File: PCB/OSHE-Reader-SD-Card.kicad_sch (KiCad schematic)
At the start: 3 parts, among them J2 112L-TDA0

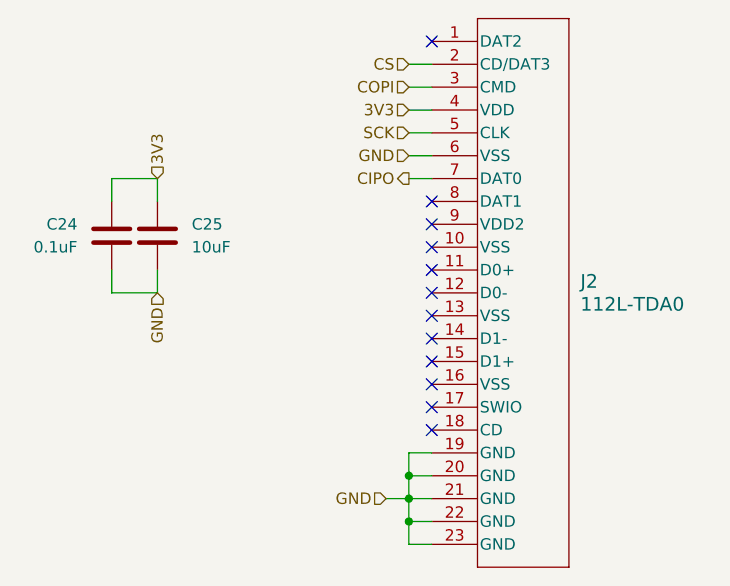
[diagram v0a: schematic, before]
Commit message: fixed battery voltage input to mcu being over 3.3V, minor changes to layout of sd card schematic
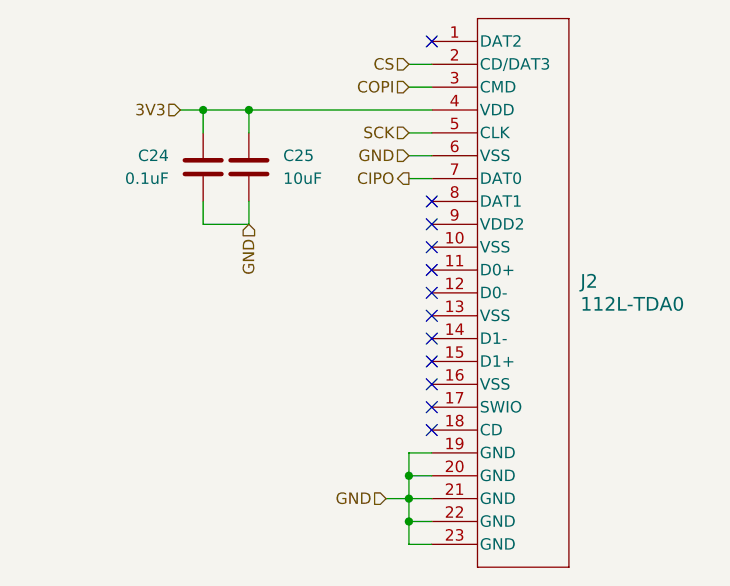
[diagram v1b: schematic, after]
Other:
- moved on the sheet: C24, C25
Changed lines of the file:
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@@
 	(paper "A4")
+	(junction
+		(at 49.53 57.15)
+		(diameter 0)
+		(color 0 0 0 0)
+	)
 	(junction
 		(at 72.39 97.79)
@@
 	)
 	(junction
+		(at 54.61 57.15)
+		(diameter 0)
+		(color 0 0 0 0)
+	)
+	(junction
 		(at 72.39 100.33)
 		(diameter 0)
@@
 	(wire
 		(pts
-			(xy 44.45 74.93) (xy 44.45 77.47)
+			(xy 49.53 67.31) (xy 49.53 69.85)
+		)
+		(stroke
+			(width 0)
+			(type default)
+		)
+	)
+	(wire
+		(pts
+			(xy 49.53 57.15) (xy 54.61 57.15)
 		)
 		(stroke
@@
 	(wire
 		(pts
-			(xy 39.37 67.31) (xy 39.37 64.77)
+			(xy 54.61 57.15) (xy 74.93 57.15)
 		)
 		(stroke
@@
 	(wire
 		(pts
-			(xy 39.37 77.47) (xy 44.45 77.47)
-		)
-		(stroke
-			(width 0)
-			(type default)
-		)
-	)
-	(wire
-		(pts
 			(xy 69.85 100.33) (xy 72.39 100.33)
 		)
@@
 	(wire
 		(pts
-			(xy 39.37 64.77) (xy 44.45 64.77)
+			(xy 54.61 67.31) (xy 54.61 69.85)
 		)
 		(stroke
@@
 	(wire
 		(pts
-			(xy 72.39 57.15) (xy 74.93 57.15)
-		)
-		(stroke
-			(width 0)
-			(type default)
-		)
-	)
-	(wire
-		(pts
-			(xy 44.45 64.77) (xy 44.45 67.31)
+			(xy 49.53 69.85) (xy 54.61 69.85)
+		)
+		(stroke
+			(width 0)
+			(type default)
+		)
+	)
+	(wire
+		(pts
+			(xy 54.61 57.15) (xy 54.61 59.69)
+		)
+		(stroke
+			(width 0)
+			(type default)
+		)
+	)
+	(wire
+		(pts
+			(xy 49.53 59.69) (xy 49.53 57.15)
+		)
+		(stroke
+			(width 0)
+			(type default)
+		)
+	)
+	(wire
+		(pts
+			(xy 46.99 57.15) (xy 49.53 57.15)
 		)
 		(stroke
@@
 	(wire
 		(pts
-			(xy 39.37 74.93) (xy 39.37 77.47)
-		)
-		(stroke
-			(width 0)
-			(type default)
-		)
-	)
-	(wire
-		(pts
 			(xy 72.39 59.69) (xy 74.93 59.69)
 		)
@@
 		)
 	)
+	(hierarchical_label "GND"
+		(shape input)
+		(at 54.61 69.85 270)
+		(effects
+			(font
+				(size 1.27 1.27)
+			)
+			(justify right)
+		)
+	)
 	(hierarchical_label "CS"
 		(shape input)
@@
 		)
 	)
-	(hierarchical_label "3V3"
-		(shape input)
-		(at 44.45 64.77 90)
-		(effects
-			(font
-				(size 1.27 1.27)
-			)
-			(justify left)
-		)
-	)
 	(hierarchical_label "GND"
 		(shape input)
@@
 		(shape input)
 		(at 69.85 100.33 180)
-		(effects
-			(font
-				(size 1.27 1.27)
-			)
-			(justify right)
-		)
-	)
-	(hierarchical_label "GND"
-		(shape input)
-		(at 44.45 77.47 270)
 		(effects
 			(font
@@
 	(hierarchical_label "3V3"
 		(shape input)
-		(at 72.39 57.15 180)
+		(at 46.99 57.15 180)
 		(effects
 			(font
@@
 	(symbol
 		(lib_id "Device:C")
-		(at 39.37 71.12 0)
+		(at 49.53 63.5 0)
 		(mirror y)
 		(unit 1)
@@
 		(dnp no)
 		(property "Reference" "C24"
-			(at 35.56 69.8499 0)
+			(at 45.72 62.2299 0)
 			(effects
 				(font
@@
 		)
 		(property "Value" "0.1uF"
-			(at 35.56 72.3899 0)
+			(at 45.72 64.7699 0)
 			(effects
 				(font
@@
 		)
 		(property "Footprint" ""
-			(at 38.4048 74.93 0)
+			(at 48.5648 67.31 0)
 			(effects
 				(font
@@
 		)
 		(property "Datasheet" "~"
-			(at 39.37 71.12 0)
+			(at 49.53 63.5 0)
 			(effects
 				(font
@@
 		)
 		(property "Description" "Unpolarized capacitor"
-			(at 39.37 71.12 0)
+			(at 49.53 63.5 0)
 			(effects
 				(font
@@
 	(symbol
 		(lib_id "Device:C")
-		(at 44.45 71.12 0)
+		(at 54.61 63.5 0)
 		(unit 1)
 		(exclude_from_sim no)
@@
 		(fields_autoplaced yes)
 		(property "Reference" "C25"
-			(at 48.26 69.8499 0)
+			(at 58.42 62.2299 0)
 			(effects
 				(font
@@
 		)
 		(property "Value" "10uF"
-			(at 48.26 72.3899 0)
+			(at 58.42 64.7699 0)
 			(effects
 				(font
@@
 		)
 		(property "Footprint" ""
-			(at 45.4152 74.93 0)
+			(at 55.5752 67.31 0)
 			(effects
 				(font
@@
 		)
 		(property "Datasheet" "~"
-			(at 44.45 71.12 0)
+			(at 54.61 63.5 0)
 			(effects
 				(font
@@
 		)
 		(property "Description" "Unpolarized capacitor"
-			(at 44.45 71.12 0)
+			(at 54.61 63.5 0)
 			(effects
 				(font
@@
 		)
 		(instances
-			(project ""
+			(project "OSHE-Reader-PCB"
 				(path "/3f072c92-e35a-4654-839b-728bd3dc3a46/f673c940-d558-4160-83eb-d33ca6356616"
 					(reference "C25")

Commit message: Footprints added
All footprints added (problem with J1 for some reason) ((pads of the display driver))
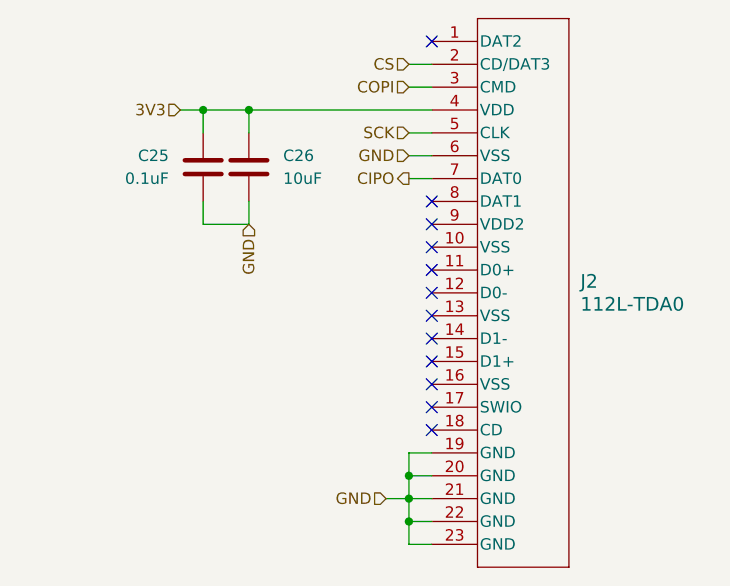
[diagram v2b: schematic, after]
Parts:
- C25: renamed from C24; footprint (none) -> Capacitor_SMD:C_1206_3216Metric
- C26: renamed from C25; footprint (none) -> Capacitor_SMD:C_1206_3216Metric
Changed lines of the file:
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@@
 		(on_board yes)
 		(dnp no)
-		(property "Reference" "C24"
+		(property "Reference" "C25"
 			(at 45.72 62.2299 0)
 			(effects
@@
 			)
 		)
-		(property "Footprint" ""
+		(property "Footprint" "Capacitor_SMD:C_1206_3216Metric"
 			(at 48.5648 67.31 0)
 			(effects
@@
 		)
 		(instances
+			(project "OSHE-Reader-SD-Card"
+				(path "/276472ca-f1d7-4a72-a9b0-d2661de39226"
+					(reference "C25")
+					(unit 1)
+				)
+			)
 			(project "OSHE-Reader-PCB"
 				(path "/3f072c92-e35a-4654-839b-728bd3dc3a46/f673c940-d558-4160-83eb-d33ca6356616"
@@
 		)
 		(instances
+			(project "OSHE-Reader-SD-Card"
+				(path "/276472ca-f1d7-4a72-a9b0-d2661de39226"
+					(reference "J2")
+					(unit 1)
+				)
+			)
 			(project ""
 				(path "/3f072c92-e35a-4654-839b-728bd3dc3a46/f673c940-d558-4160-83eb-d33ca6356616"
@@
 		(dnp no)
 		(fields_autoplaced yes)
-		(property "Reference" "C25"
+		(property "Reference" "C26"
 			(at 58.42 62.2299 0)
 			(effects
@@
 			)
 		)
-		(property "Footprint" ""
+		(property "Footprint" "Capacitor_SMD:C_1206_3216Metric"
 			(at 55.5752 67.31 0)
 			(effects
@@
 		)
 		(instances
+			(project "OSHE-Reader-SD-Card"
+				(path "/276472ca-f1d7-4a72-a9b0-d2661de39226"
+					(reference "C26")
+					(unit 1)
+				)
+			)
 			(project "OSHE-Reader-PCB"
 				(path "/3f072c92-e35a-4654-839b-728bd3dc3a46/f673c940-d558-4160-83eb-d33ca6356616"
@@
 		)
 	)
+	(sheet_instances
+		(path "/"
+			(page "1")
+		)
+	)
+	(embedded_fonts no)
 )

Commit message: Did a bunch of work with final preparations of the schematic for pcb routing
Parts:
- renumbered C25 to C24, C26 to C25
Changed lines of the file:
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@@
 		(on_board yes)
 		(dnp no)
-		(property "Reference" "C25"
+		(property "Reference" "C24"
 			(at 45.72 62.2299 0)
 			(effects
@@
 		(dnp no)
 		(fields_autoplaced yes)
-		(property "Reference" "C26"
+		(property "Reference" "C25"
 			(at 58.42 62.2299 0)
 			(effects
